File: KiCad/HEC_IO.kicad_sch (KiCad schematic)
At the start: 21 parts, among them J2 Conn_02x03_Odd_Even, SW1 SW_DIP_x04, U12 74LS04, U17 74LS20, U22 74LS02, U30 74LS74, U31 74LS32, U32 LM79M05_TO220, U33 74LS20, U34 74LS393, U6 74LS138

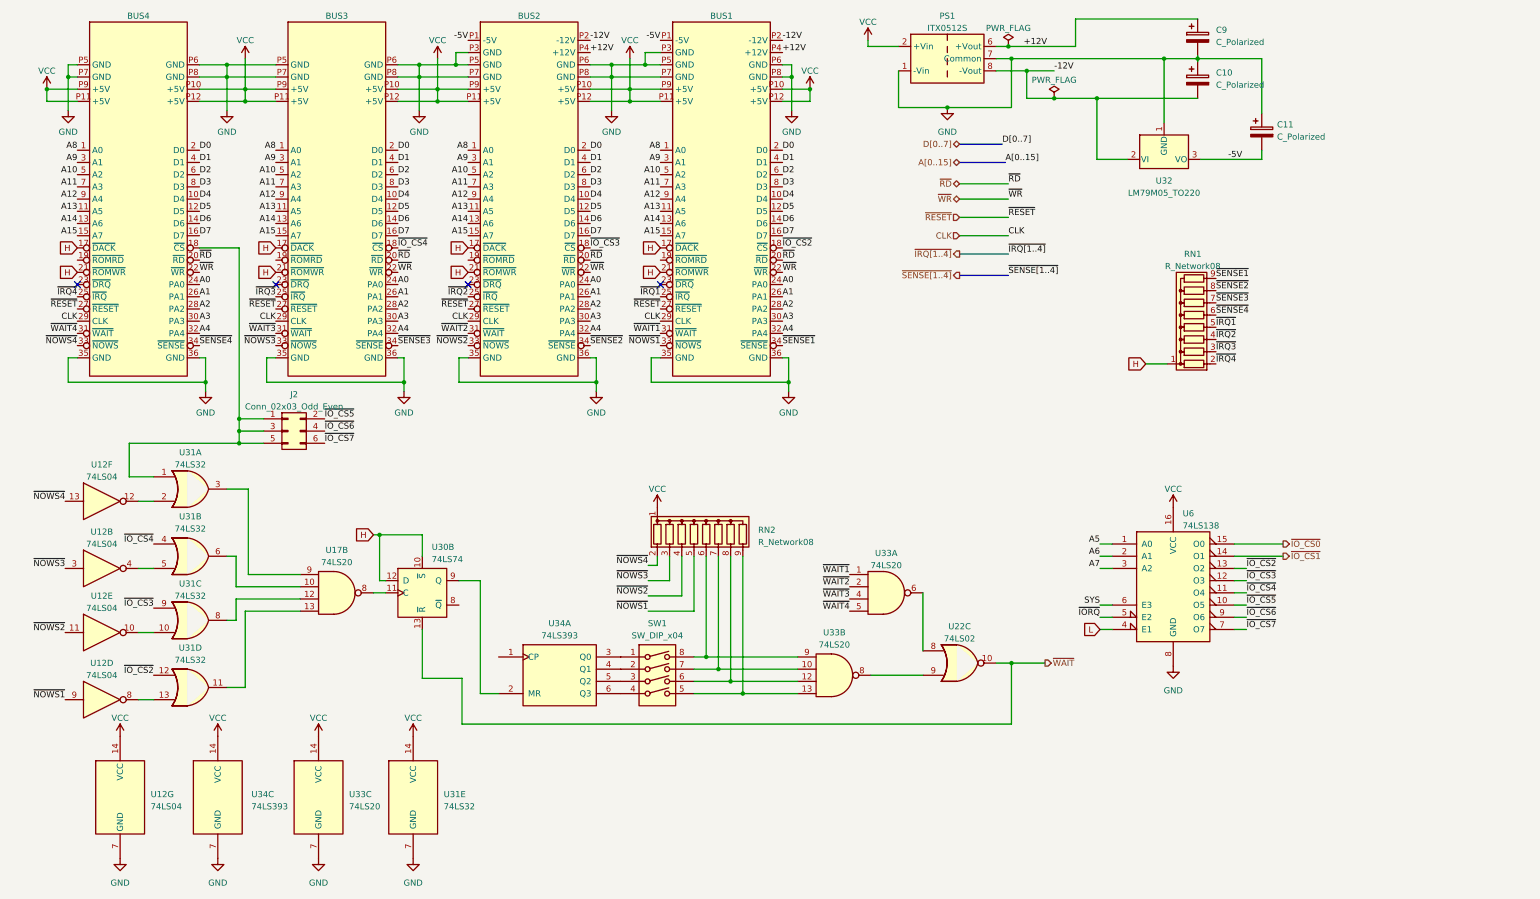
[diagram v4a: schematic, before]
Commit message: Saved changes for added save state generator
Some changes for the wait state generator was not saved in the last commit
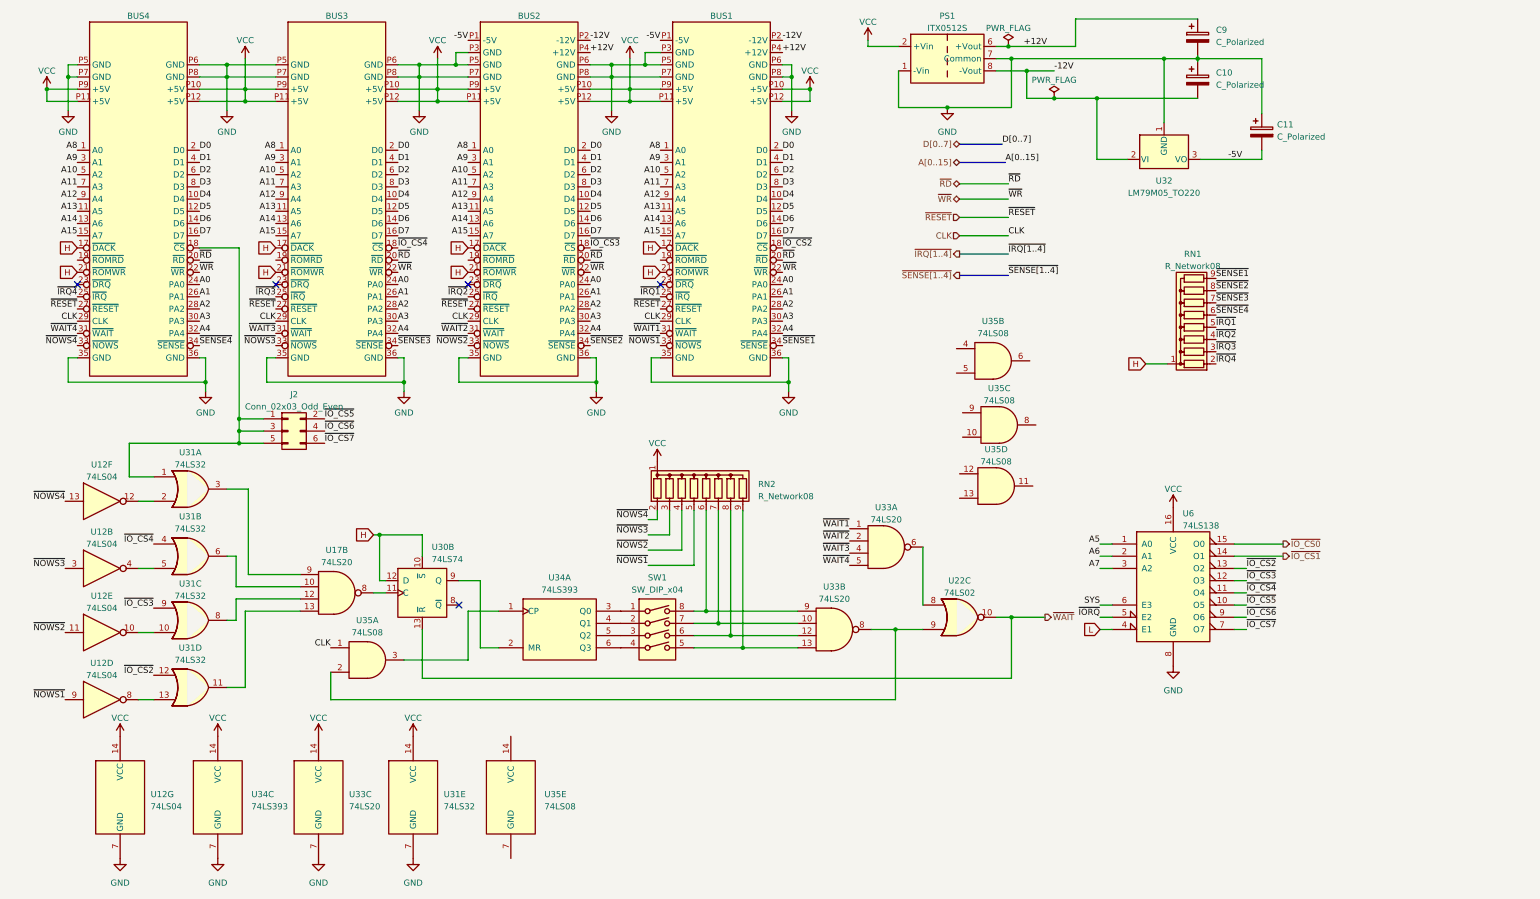
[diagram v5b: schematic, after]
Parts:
- added U35: 74LS08, symbol 74xx:74LS08
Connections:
- net CLK: now also U35.1
- net at U22.9, U33.8: now also U35.2
- net at U34.1 (CP): now also U35.3
- no-connect marks 4 -> 5
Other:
- moved on the sheet: RN2, SW1, U22C, U33A, U33B, U34A

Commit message: MATX-compliant motherboard
Made the motherboard mounting holes and card positions MATX compliant. The MATX motherboard edge is shifted 0.5 inches to the left, which is annoying. Also, cards have component on the opposite side from ISA, meaning PCI slot positioning must be followed. However, PCI pins are not 0.1inch apart, so lining up is tricky. I don't know whether I got it right.
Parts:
- added J4: Conn_02x13_Odd_Even, Connector_PinHeader_2.54mm:PinHeader_2x13_P2.54mm_Vertical, symbol Connector_Generic:Conn_02x13_Odd_Even
- added U36: 74LS27, Package_DIP:DIP-14_W7.62mm_Socket, symbol 74xx:74LS27
- J2: footprint (none) -> Connector_PinHeader_2.54mm:PinHeader_2x03_P2.54mm_Vertical
- U17, U31, U33, U34, U35: footprint (none) -> Package_DIP:DIP-14_W7.62mm_Socket
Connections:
- net A0: now also J4.7 (Pin_7)
- net A1: now also J4.9 (Pin_9)
- net A2: now also J4.11 (Pin_11)
- net A3: now also J4.13 (Pin_13)
- net A4: now also J4.15 (Pin_15)
- net D0: now also J4.2 (Pin_2)
- net D1: now also J4.4 (Pin_4)
- net D2: now also J4.6 (Pin_6)
- net D3: now also J4.8 (Pin_8)
- net D4: now also J4.10 (Pin_10)
- net D5: now also J4.12 (Pin_12)
- net D6: now also J4.14 (Pin_14)
- net D7: now also J4.16 (Pin_16)
- net GND: now also J4.26 (Pin_26)
- net VCC: now also J4.22 (Pin_22), J4.24 (Pin_24)
- net ~{IO_CS1}: now also J4.1 (Pin_1)
- net ~{RD}: now also J4.3 (Pin_3)
- net ~{RESET}: now also J4.17 (Pin_17)
- net ~{WAIT}: now also U36.12; no longer U22.10
- net ~{WR}: now also J4.5 (Pin_5)
- net at U22.8: no longer U33.6
- net at U33.8, U35.2: now also U36.13; no longer U22.9
- net CLK renamed OSC
- net OSC: now also J4.20 (Pin_20)
- new net: U33.6, U36.2
- new net WAIT_INTERNAL: J4.18 (Pin_18), U36.1
- new net ~{KB_INT}: J4.23 (Pin_23)
- new net ~{MS_INT}: J4.25 (Pin_25)
- new net ~{PSG_INT}: J4.21 (Pin_21)
- new net ~{VDP_INT}: J4.19 (Pin_19)
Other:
- moved on the sheet: U22C, U33A, U35B, U35C, U35D

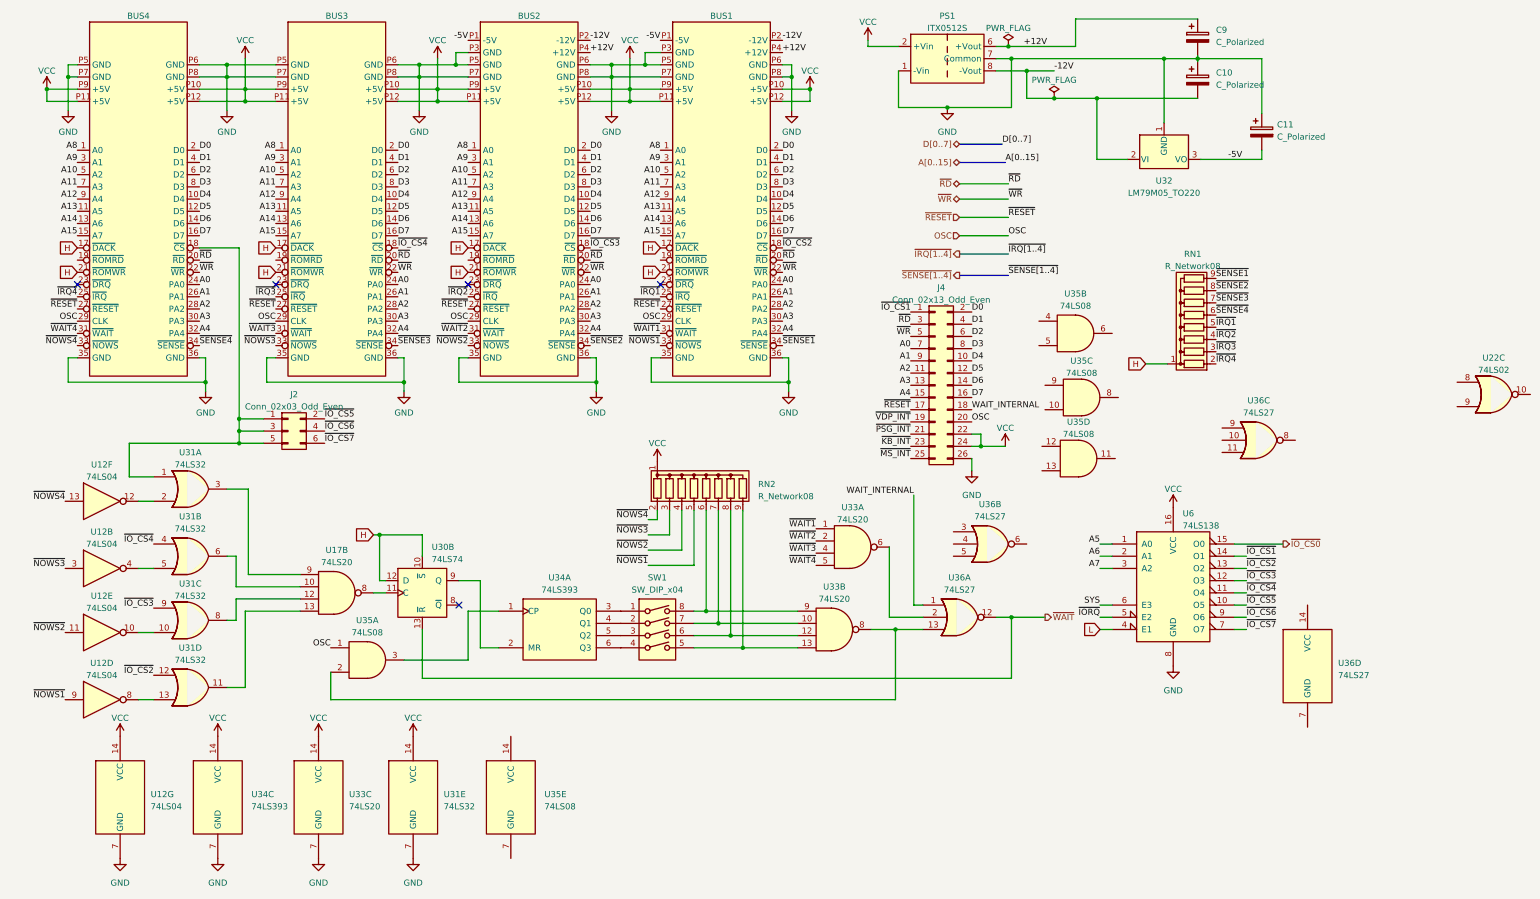
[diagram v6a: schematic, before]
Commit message: PCB Update
Some part placement, some routing, some change in schematic for easier PCB routing.
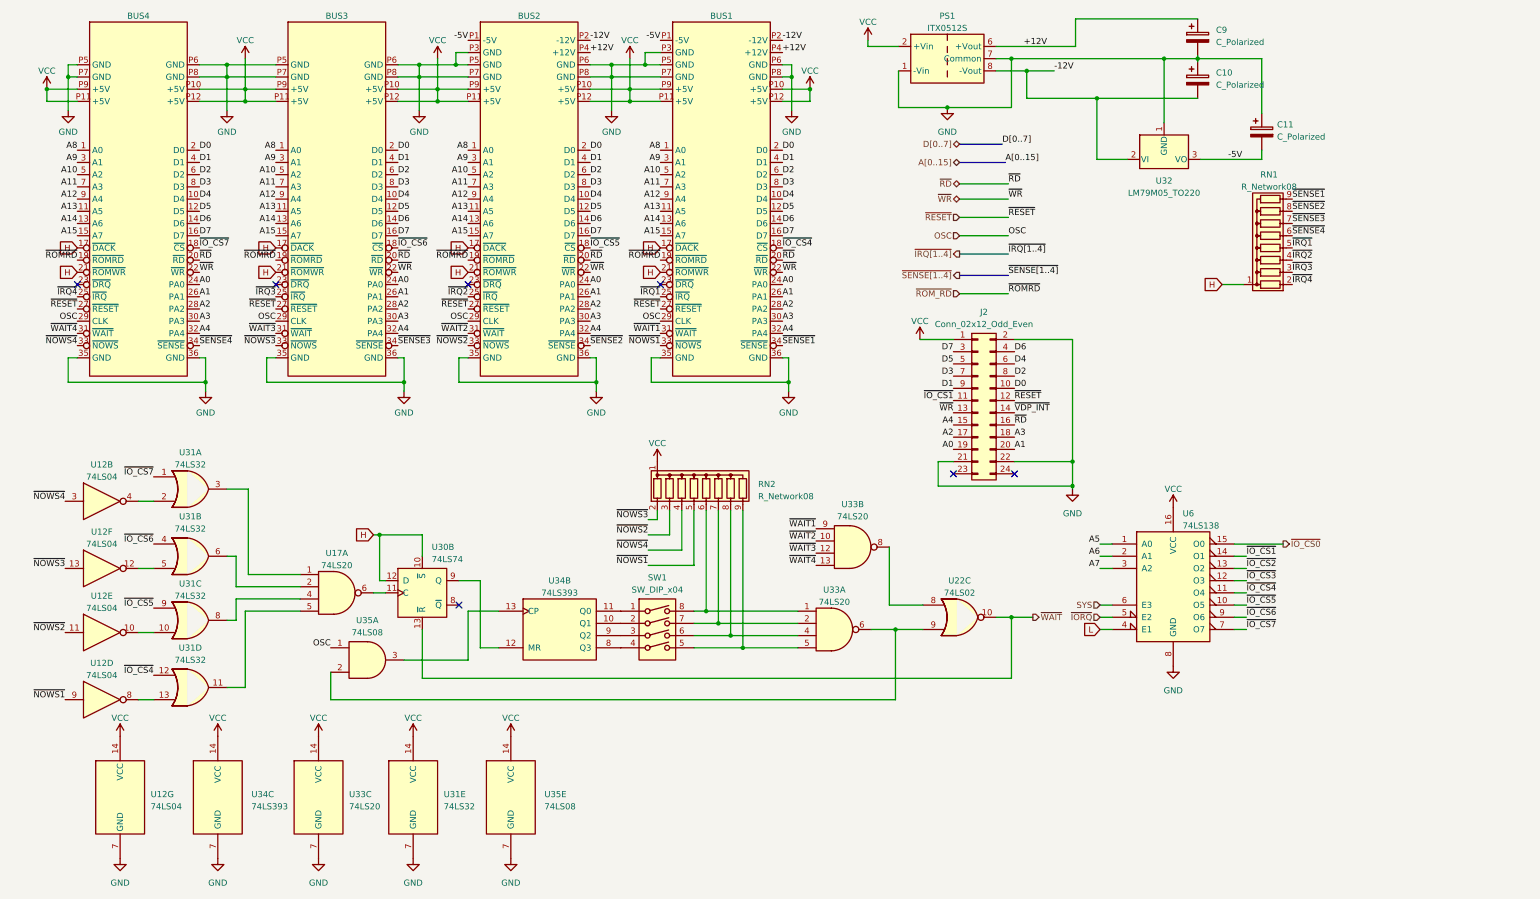
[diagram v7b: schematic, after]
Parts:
- removed J2: Conn_02x03_Odd_Even, Connector_PinHeader_2.54mm:PinHeader_2x03_P2.54mm_Vertical, symbol Connector_Generic:Conn_02x03_Odd_Even
- removed J4: Conn_02x13_Odd_Even, Connector_PinHeader_2.54mm:PinHeader_2x13_P2.54mm_Vertical, symbol Connector_Generic:Conn_02x13_Odd_Even
- removed U17: 74LS20, Package_DIP:DIP-14_W7.62mm_Socket, symbol 74xx:74LS20
- removed unit 1 of U34
- removed unit 2 of U35
- removed unit 4 of U35
- removed unit 3 of U35
- removed U36: 74LS27, Package_DIP:DIP-14_W7.62mm_Socket, symbol 74xx:74LS27
- added J2: Conn_02x12_Odd_Even, symbol Connector_Generic:Conn_02x12_Odd_Even
- added U17: 74LS20, Package_DIP:DIP-14_W7.62mm_Socket, symbol 74xx:74LS20
- added unit 2 of U34
- C10, C11, C9: footprint (none) -> Capacitor_THT:CP_Radial_D6.3mm_P2.50mm
- SW1: footprint (none) -> Button_Switch_THT:SW_DIP_SPSTx04_Slide_9.78x12.34mm_W7.62mm_P2.54mm
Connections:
- net A0: now also J2.19 (Pin_19)
- net A1: now also J2.20 (Pin_20)
- net A2: now also J2.17 (Pin_17)
- net A3: now also J2.18 (Pin_18)
- net A4: now also J2.15 (Pin_15)
- net D0: now also J2.10 (Pin_10)
- net D1: now also J2.9 (Pin_9)
- net D2: now also J2.8 (Pin_8)
- net D3: now also J2.7 (Pin_7)
- net D4: now also J2.6 (Pin_6)
- net D5: now also J2.5 (Pin_5)
- net D6: now also J2.4 (Pin_4)
- net D7: now also J2.3 (Pin_3)
- net GND: now also U35.7 (GND), J2.2 (Pin_2), J2.21 (Pin_21), J2.22 (Pin_22)
- net VCC: now also U35.14 (VCC), J2.1 (Pin_1)
- net ~{IO_CS1}: now also J2.11 (Pin_11)
- net ~{IO_CS2}: no longer BUS1.18 (~{CS}), U31.12
- net ~{IO_CS3}: no longer BUS2.18 (~{CS}), U31.9
- net ~{IO_CS4}: now also BUS1.18 (~{CS}), U31.12; no longer BUS3.18 (~{CS}), U31.4
- net ~{IO_CS5}: now also BUS2.18 (~{CS}), U31.9
- net ~{IO_CS6}: now also BUS3.18 (~{CS}), U31.4
- net ~{IO_CS7}: now also BUS4.18 (~{CS}), U31.1
- net ~{NOWS2}: now also RN2.3 (R2); no longer RN2.4 (R3)
- net ~{NOWS3}: now also RN2.2 (R1), U12.13; no longer RN2.3 (R2), U12.3
- net ~{NOWS4}: now also RN2.4 (R3), U12.3; no longer RN2.2 (R1), U12.13
- net ~{RD}: now also J2.16 (Pin_16)
- net ~{RESET}: now also J2.12 (Pin_12)
- net ~{VDP_INT}: now also J2.14 (Pin_14)
- net ~{WAIT1}: now also U33.9; no longer U33.1
- net ~{WAIT2}: now also U33.10; no longer U33.2
- net ~{WAIT3}: now also U33.12; no longer U33.4
- net ~{WAIT4}: now also U33.13; no longer U33.5
- net ~{WAIT}: now also U22.10
- net ~{WR}: now also J2.13 (Pin_13)
- net at U22.8: now also U33.8
- net at U22.9: now also U33.6, U35.2
- net ~{ROM_RD}: now reaches BUS2.19 (~{ROMRD})
- net ~{ROM_RD}: now also BUS1.19 (~{ROMRD}), BUS3.19 (~{ROMRD}), BUS4.19 (~{ROMRD})
- net at U35.3: now also U34.13 (CP)
- net at U30.9 (Q): now also U34.12 (MR)
- net at SW1.1: now also U34.11 (Q0)
- net at SW1.2: now also U34.10 (Q1)
- net at SW1.3: now also U34.9 (Q2)
- net at SW1.4: now also U34.8 (Q3)
- net at U31.2: now also U12.4; no longer U12.12
- net at U31.3: now also U17.1
- net at RN2.9 (R8), SW1.5: now also U33.5; no longer U33.13
- net at RN2.8 (R7), SW1.6: now also U33.4; no longer U33.12
- net at RN2.7 (R6), SW1.7: now also U33.2; no longer U33.10
- net at RN2.6 (R5), SW1.8: now also U33.1; no longer U33.9
- net at U30.11 (C): now also U17.6
- net at U31.11: now also U17.5
- net at U31.6: now also U17.2
- net at U31.8: now also U17.4
- net at U31.5: now also U12.12; no longer U12.4
- no-connect marks 5 -> 7
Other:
- moved on the sheet: RN1, U12B, U12F, U22C, U33A, U33B

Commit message: Add POST code circuit
Add circuit to show POST code using I register on Z80 to assist debugging.
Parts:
- J2: footprint (none) -> Connector_PinHeader_2.54mm:PinHeader_2x12_P2.54mm_Vertical
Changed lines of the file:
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@@
       (effects (font (size 1.27 1.27)))
     )
-    (property "Footprint" "" (at 209.55 95.25 0)
+    (property "Footprint" "Connector_PinHeader_2.54mm:PinHeader_2x12_P2.54mm_Vertical" (at 209.55 95.25 0)
       (effects (font (size 1.27 1.27)) hide)
     )
